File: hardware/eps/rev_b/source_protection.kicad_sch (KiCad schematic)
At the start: 39 parts, among them Q600 IRLR2908, Q601 IRLR2908, Q602 MMBT3906LT1G, U600 LTC4364HDE-2

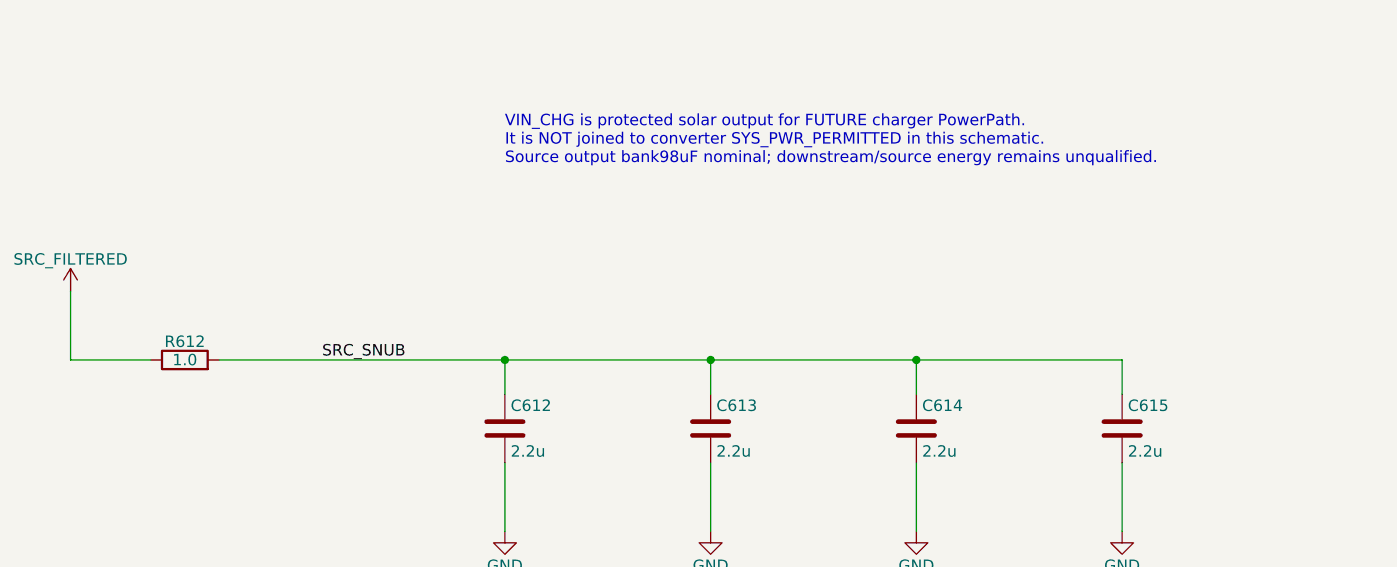
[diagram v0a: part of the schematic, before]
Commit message: Integrate LTC4162 charger PowerPath and thermistor interface into EPS Rev B
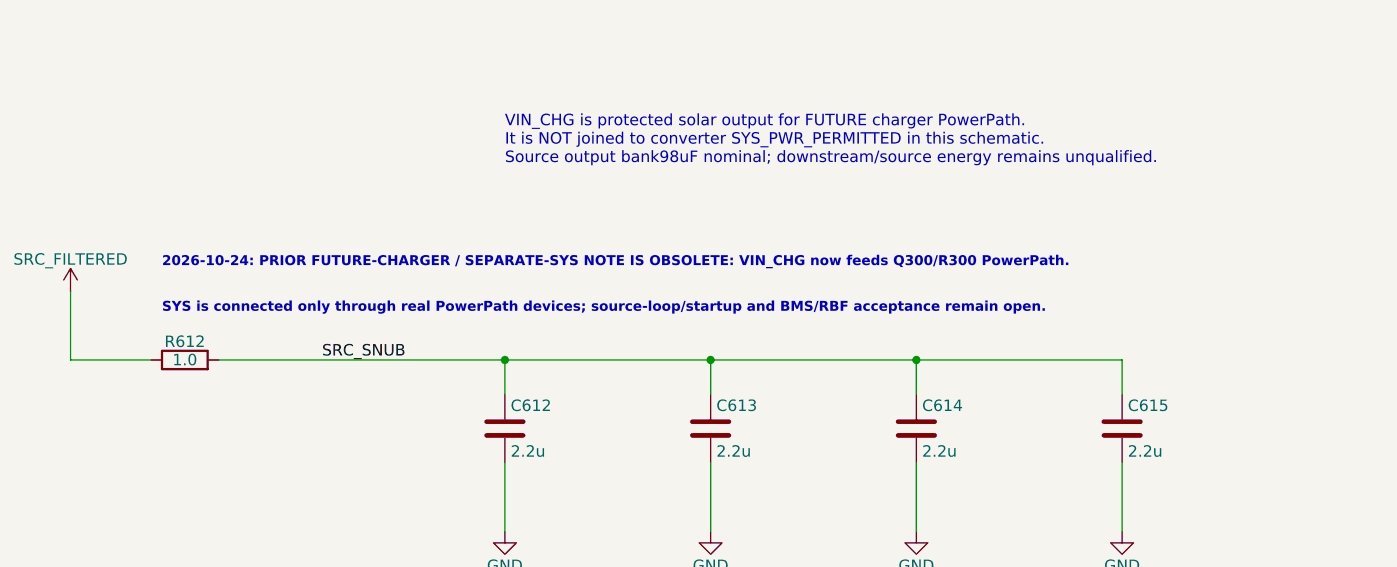
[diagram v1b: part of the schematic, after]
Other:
- note added: "2026-10-24: PRIOR FUTURE-CHARGER / SEPARATE-SYS NOTE IS OBSOLETE: VIN_CHG now feeds Q300/R300 PowerPath."
- note added: "SYS is connected only through real PowerPath devices; source-loop/startup and BMS/RBF acceptance remain open."
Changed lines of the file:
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@@
 		)
 	)
+  (text "2026-10-24: PRIOR FUTURE-CHARGER / SEPARATE-SYS NOTE IS OBSOLETE: VIN_CHG now feeds Q300/R300 PowerPath."
+    (at 175.26 229.87 0)
+    (effects (font (size 1.1 1.1) (bold yes)) (justify left bottom))
+  )
+  (text "SYS is connected only through real PowerPath devices; source-loop/startup and BMS/RBF acceptance remain open."
+    (at 175.26 234.95 0)
+    (effects (font (size 1.1 1.1) (bold yes)) (justify left bottom))
+  )
 	(symbol
 		(lib_id "Power_Management:LTC4364HDE")

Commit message: Integrate EPS Rev B battery management development circuit
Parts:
- R601, R610, R612: TCR 25 ppm/K -> 100 ppm/K
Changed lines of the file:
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@@
 			)
 		)
-		(property "TCR" "25 ppm/K"
+		(property "TCR" "100 ppm/K"
 			(at 43.18 102.87 0)
 			(hide yes)
@@
 			)
 		)
-		(property "TCR" "25 ppm/K"
+		(property "TCR" "100 ppm/K"
 			(at 299.72 176.53 0)
 			(hide yes)
@@
 			)
 		)
-		(property "TCR" "25 ppm/K"
+		(property "TCR" "100 ppm/K"
 			(at 177.8 240.03 0)
 			(hide yes)
